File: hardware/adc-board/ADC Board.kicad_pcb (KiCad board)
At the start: 4 copper layers, 92.7 x 83.8 mm, 123 parts, among them J1 BHR-44-HUA, J10 BootJumper, J11 USB Header, J2 ST-LINK/V2, J3 USART3, J4 USART1, J5 UE27AC5410H, J6 54601-908WPLF, J7 AltPowerInput, J8 USBPowerJumper, J9 USART2, U0 STM32H743ZITx, U1 Opamp_Quad_Generic, U10 MCP1501T-20E/CHY, U13 3.3V Reg, U14 ISL83490, U2 Opamp_Quad_Generic, U29 AP2114HA-3.3TRG1, U3 Opamp_Quad_Generic, U4 Opamp_Quad_Generic, U5 Opamp_Quad_Generic, U6 Opamp_Quad_Generic, U7 MCP120-xxxxTT, U9 USBLC6-2SC6

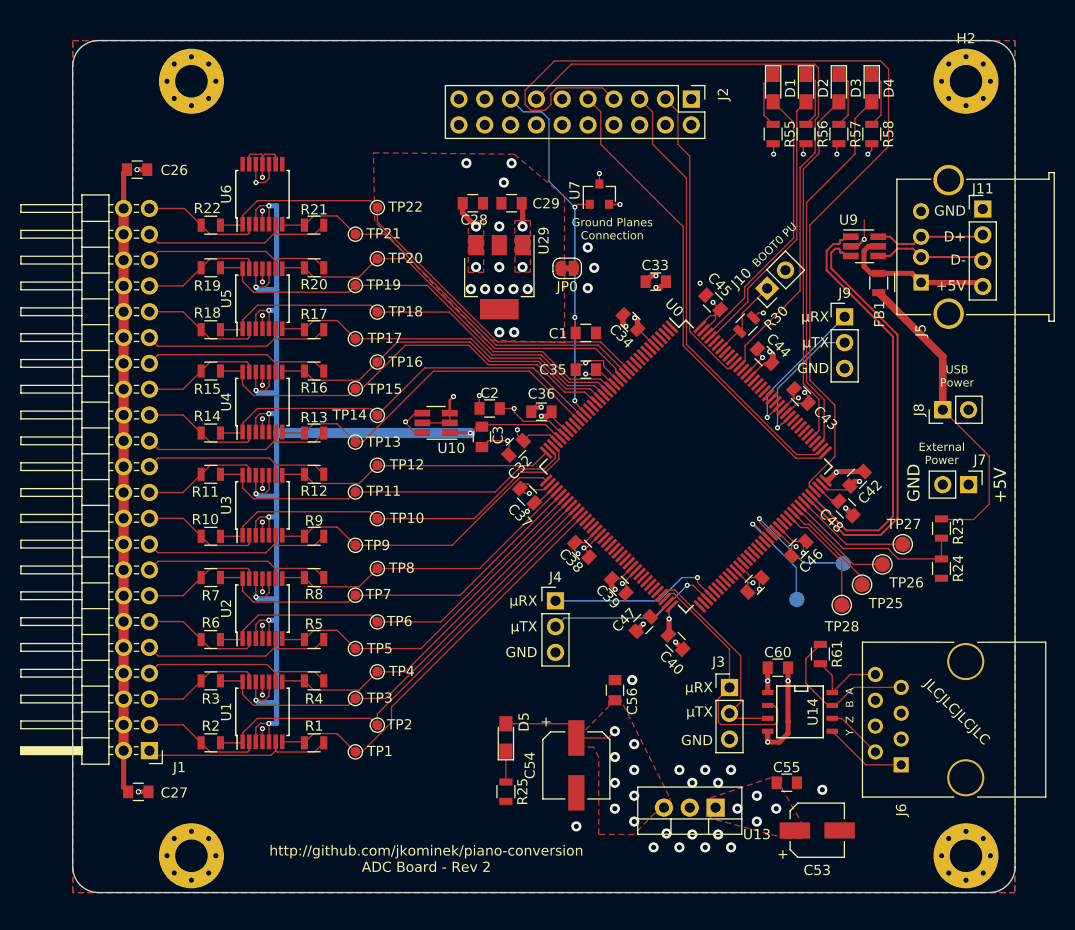
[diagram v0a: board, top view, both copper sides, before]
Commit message: Unified ground nets in schematic and layout.
* Rearranged the layers that pours are on.
* Added the keep-out zone separating analog and
  digital areas from each other.
* Tightened up placement of decoupling capacitors.
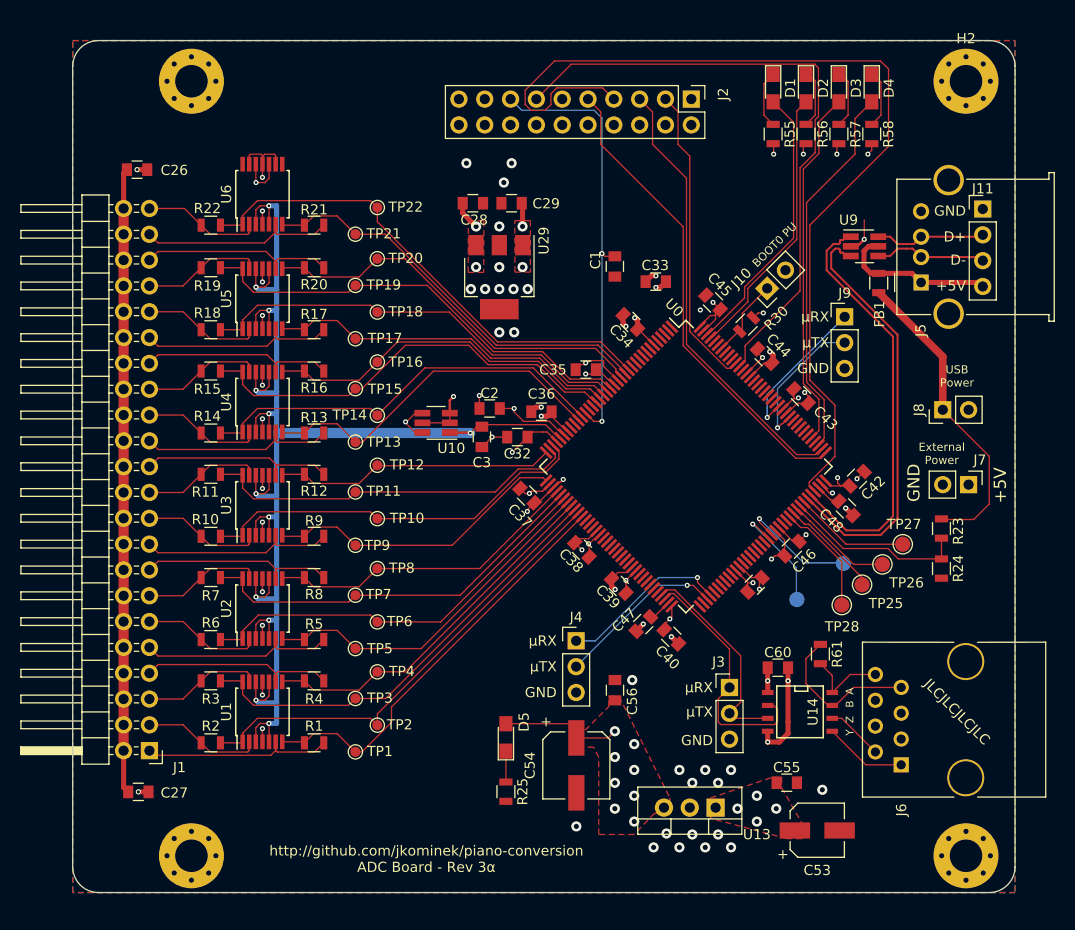
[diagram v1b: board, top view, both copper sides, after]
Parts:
- removed JP0: SolderJumper_2_Bridged, Jumper:SolderJumper-2_P1.3mm_Bridged_RoundedPad1.0x1.5mm
- removed U7: MCP120-xxxxTT, TO_SOT_Packages_SMD:SOT-23
- moved C1 7.14 mm to (85.1, 69.2), turned to -90 degrees
- moved J4 4.43 mm to (81.3, 106.0)
- moved C32 1.07 mm to (75.5, 86.0), turned to 180 degrees
- moved C46 0.68 mm to (102.5, 97.0)
- moved C40 0.67 mm to (90.6, 105.6)
- turned C42 to 45 degrees
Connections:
- C1 pad 2: GNDD -> GND
- C2 pad 2: GNDA -> GND
- C26 pad 1: GNDA -> GND
- C27 pad 1: GNDA -> GND
- C28 pad 2: GNDA -> GND
- C29 pad 2: GNDA -> GND
- C3 pad 2: GNDA -> GND
- C32 pad 2: GNDA -> GND
- C33 pad 2: GNDD -> GND
- C34 pad 2: GNDD -> GND
- C35 pad 2: GNDD -> GND
- C36 pad 2: GNDD -> GND
- C37 pad 2: GNDD -> GND
- C38 pad 2: GNDD -> GND
- C39 pad 2: GNDD -> GND
- C40 pad 2: GNDD -> GND
- C41 pad 2: GNDD -> GND
- C42 pad 2: GNDD -> GND
- C43 pad 2: GNDD -> GND
- C44 pad 2: GNDD -> GND
- C45 pad 2: GNDD -> GND
- C46 pad 2: GNDD -> GND
- C47 pad 2: GNDD -> GND
- C48 pad 2: GNDD -> GND
- C53 pad 2: GNDD -> GND
- C54 pad 2: GNDD -> GND
- C55 pad 2: GNDD -> GND
- C56 pad 2: GNDD -> GND
- C60 pad 2: GNDD -> GND
- H1 pad 1: GNDD -> GND
- H2 pad 1: GNDD -> GND
- H3 pad 1: GNDD -> GND
- H4 pad 1: GNDD -> GND
- J11 pad 1: GNDD -> GND
- J2 pad 10: GNDD -> GND
- J2 pad 12: GNDD -> GND
- J2 pad 14: GNDD -> GND
- J2 pad 16: GNDD -> GND
- J2 pad 18: GNDD -> GND
- J2 pad 20: GNDD -> GND
- J2 pad 4: GNDD -> GND
- J2 pad 6: GNDD -> GND
- J2 pad 8: GNDD -> GND
- J3 pad 3: GNDD -> GND
- J4 pad 3: GNDD -> GND
- J5 pad 4: GNDD -> GND
- J5 pad 5: GNDD -> GND
- J6 pad 4: GNDD -> GND
- J6 pad 6: GNDD -> GND
- J7 pad 2: GNDD -> GND
- J9 pad 3: GNDD -> GND
- R24 pad 2: GNDD -> GND
- R25 pad 2: GNDD -> GND
- R30 pad 2: GNDD -> GND
- R55 pad 2: GNDD -> GND
- R56 pad 2: GNDD -> GND
- R57 pad 2: GNDD -> GND
- R58 pad 2: GNDD -> GND
- U0 pad 107: GNDD -> GND
- U0 pad 120: GNDD -> GND
- U0 pad 130: GNDD -> GND
- U0 pad 16: GNDD -> GND
- U0 pad 31: GNDA -> GND
- U0 pad 38: GNDD -> GND
- U0 pad 51: GNDD -> GND
- U0 pad 61: GNDD -> GND
- U0 pad 83: GNDD -> GND
- U0 pad 94: GNDD -> GND
- U1 pad 11: GNDA -> GND
- U10 pad 2: GNDA -> GND
- U10 pad 3: GNDA -> GND
- U10 pad 5: GNDA -> GND
- U13 pad 2: GNDD -> GND
- U14 pad 4: GNDD -> GND
- U2 pad 11: GNDA -> GND
- U29 pad 2: GNDA -> GND
- U3 pad 11: GNDA -> GND
- U4 pad 11: GNDA -> GND
- U5 pad 11: GNDA -> GND
- U6 pad 11: GNDA -> GND
- U6 pad 13: GNDA -> GND
- U6 pad 9: GNDA -> GND
- U9 pad 2: GNDD -> GND
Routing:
- net GND: track 0.00 -> 92.8 mm, vias 0 -> 63
- net GNDD: track 64.5 -> 0.00 mm, vias 43 -> 0
- net GNDA: track 33.2 -> 0.00 mm, vias 23 -> 0
- net /NRST: track 38.1 -> 42.9 mm, vias 3 -> 2
- net +3V3: track 65.4 -> 62.1 mm
- added copper zone on In1.Cu, net +3.3VA
- added copper zone on In1.Cu, net +3V3
- added copper zone on In2.Cu, net +5V
- added copper zone on B.Cu, net GND
- added copper zone on F.Cu, net GND
- removed copper zone on In2.Cu, net +3.3VA
- removed copper zone on In2.Cu, net +3V3
- removed copper zone on B.Cu, net +5V
- removed copper zone on F.Cu, net GNDA
- removed copper zone on In1.Cu, net GNDA
- removed copper zone on F.Cu, net GNDD
- removed copper zone on In1.Cu, net GNDD
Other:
- board text added: "http://github.com/jkominek/piano-conversion ADC Board - Rev 3α"
- board text removed: "Ground Planes Connection"
- board text removed: "http://github.com/jkominek/piano-conversion ADC Board - Rev 2"

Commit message: More ADC board rev 3 changes, per issue #47
* 4.5V regulator for phototransistors
* new 3.3V regulator for analog section
* new 2.0V precision voltage reference
* Analog voltages and their distribution rearranged
* Tidied up traces on the left hand side, everything is nice and curvy now
* Adjusted USB ESD protection to be optional and/or support other parts
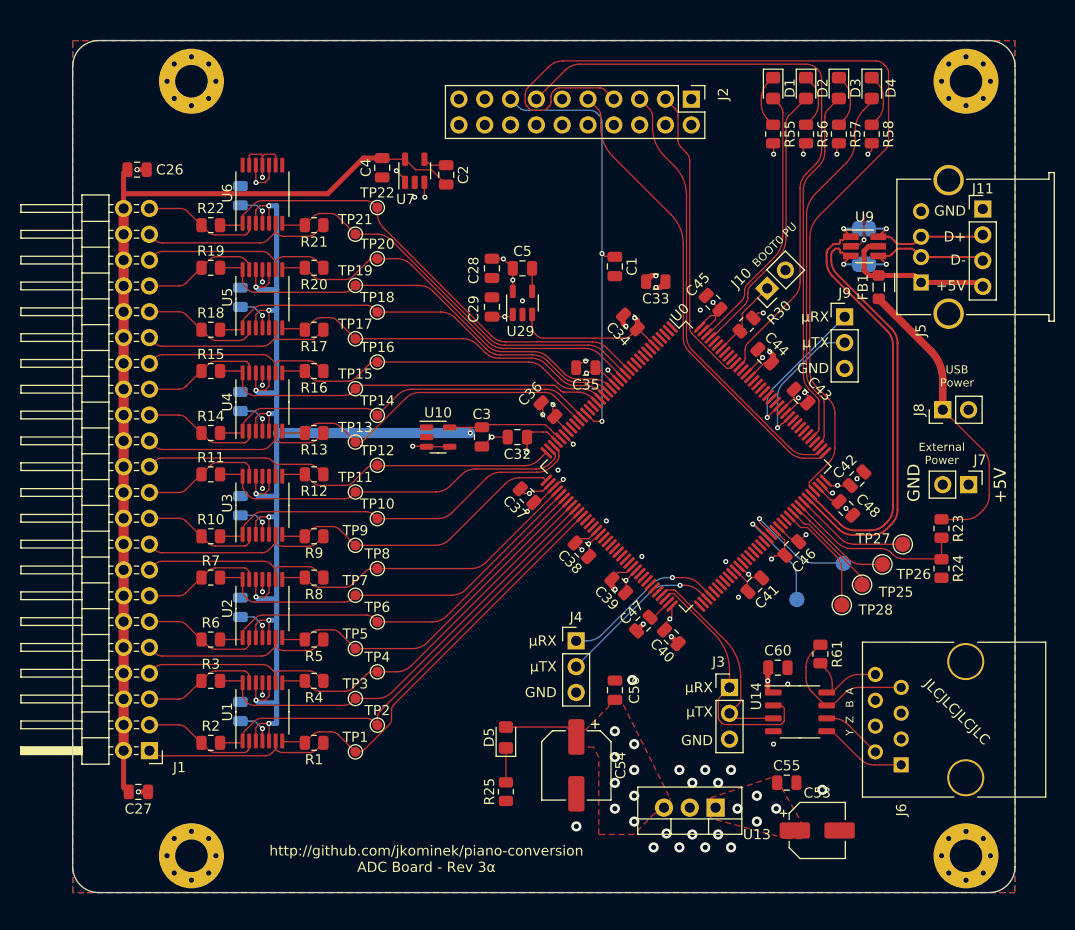
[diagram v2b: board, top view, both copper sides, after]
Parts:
- added C10: DC, Capacitor_SMD:C_0805_2012Metric, B.Cu at (48.2, 72.2)
- added C11: DC, Capacitor_SMD:C_0805_2012Metric, B.Cu at (48.2, 62.2)
- added C4: 1uF, Capacitor_SMD:C_0805_2012Metric, F.Cu at (62.2, 59.5)
- added C5: DNP, Capacitor_SMD:C_0805_2012Metric, F.Cu at (76.0, 69.4)
- added C6: DC, Capacitor_SMD:C_0805_2012Metric, B.Cu at (48.2, 113.0)
- added C7: DC, Capacitor_SMD:C_0805_2012Metric, B.Cu at (48.2, 102.8)
- added C8: DC, Capacitor_SMD:C_0805_2012Metric, B.Cu at (48.2, 92.8)
- added C9: DC, Capacitor_SMD:C_0805_2012Metric, B.Cu at (48.2, 82.5)
- added JP1: SolderJumper_2_Bridged, Jumper:SolderJumper-2_P1.3mm_Bridged_RoundedPad1.0x1.5mm, B.Cu at (109.6, 65.5)
- added JP2: SolderJumper_2_Bridged, Jumper:SolderJumper-2_P1.3mm_Bridged_RoundedPad1.0x1.5mm, B.Cu at (109.6, 69.0)
- added U7: LP2985AIM5-4.5/NOPB, Package_TO_SOT_SMD:SOT-23-5, F.Cu at (65.4, 59.8)
- C1, C26, C27, C32, C33, C34, C35, C36, C37, C38, C39, C40, C41, C42, C43, C44, C45, C46, C47, C48, C55, C56, C60: footprint Capacitors_SMD:C_0805 -> Capacitor_SMD:C_0805_2012Metric
- C2: value 2.2uF -> 1nF; footprint Capacitors_SMD:C_0805 -> Capacitor_SMD:C_0805_2012Metric
- C28, C29: value 4.7uF -> 1uF; footprint Capacitors_SMD:C_0805 -> Capacitor_SMD:C_0805_2012Metric
- C3: value 220pF -> 22nF; footprint Capacitors_SMD:C_0805 -> Capacitor_SMD:C_0805_2012Metric
- C53: footprint Capacitors_SMD:CP_Elec_5x5.3 -> Capacitor_SMD:CP_Elec_5x5.3
- C54: footprint Capacitors_SMD:CP_Elec_6.3x5.3 -> Capacitor_SMD:CP_Elec_6.3x5.3
- D1, D2, D3, D4, D5: footprint LEDs:LED_0805_HandSoldering -> LED_SMD:LED_0805_2012Metric_Pad1.15x1.40mm_HandSolder
- FB1: footprint Inductors_SMD:L_0805 -> Inductor_SMD:L_0805_2012Metric_Pad1.05x1.20mm_HandSolder
- H1, H2, H3, H4: footprint Mounting_Holes:MountingHole_3.2mm_M3_Pad_Via -> MountingHole:MountingHole_3.2mm_M3_Pad_Via
- R1, R10, R11, R12, R13, R14, R15, R16, R17, R18, R19, R2, R20, R21, R22, R23, R24, R25, R3, R30, R4, R5, R55, R56, R57, R58, R6, R61, R7, R8, R9: footprint Resistors_SMD:R_0805 -> Resistor_SMD:R_0805_2012Metric
- TP1, TP10, TP11, TP12, TP13, TP14, TP15, TP16, TP17, TP18, TP19, TP2, TP20, TP21, TP22, TP3, TP4, TP5, TP6, TP7, TP8, TP9: footprint Testpoint:TestPoint_Pad_D1.0mm -> TestPoint:TestPoint_Pad_D1.0mm
- TP23, TP24, TP25, TP26, TP27, TP28: footprint Testpoint:TestPoint_Pad_D1.5mm -> TestPoint:TestPoint_Pad_D1.5mm
- U0: footprint Housings_QFP:LQFP-144_20x20mm_Pitch0.5mm -> Package_QFP:TQFP-144_20x20mm_P0.5mm
- U1, U2, U3, U4, U5, U6: footprint Housings_SSOP:TSSOP-14_4.4x5mm_Pitch0.65mm -> Package_SO:TSSOP-14_4.4x5mm_P0.65mm
- U10: value MCP1501T-20E/CHY -> LM4120IM5-2.0/NOPB; footprint TO_SOT_Packages_SMD:SOT-23-6_Handsoldering -> Package_TO_SOT_SMD:SOT-23-5
- U14: footprint SMD_Packages:SOIC-8-N -> Package_SO:SOP-8_3.9x4.9mm_P1.27mm
- U29: value AP2114HA-3.3TRG1 -> NCP115ASN330T2G; footprint TO_SOT_Packages_SMD:SOT-223-3_TabPin2 -> Package_TO_SOT_SMD:SOT-23-5
- U9: footprint TO_SOT_Packages_SMD:SOT-23-6_Handsoldering -> Package_TO_SOT_SMD:SOT-23-6_Handsoldering
- moved C2 23.4 mm to (68.5, 60.2), turned to -90 degrees
- moved C29 10.4 mm to (73.0, 73.2), turned to 90 degrees
- moved C28 6.68 mm to (73.0, 69.4), turned to -90 degrees
- moved U29 3.40 mm to (76.0, 72.8), turned to 90 degrees
- moved U10 1.41 mm to (67.7, 86.0), turned to 0 degrees
- moved C36 0.66 mm to (78.5, 83.3), turned to 135 degrees
- moved FB1 0.41 mm to (111.0, 71.2)
- moved C35 0.19 mm to (82.2, 79.2)
- turned U14 to 0 degrees
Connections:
- C2 pad 1: +3.3VA -> Net-(C2-Pad1)
- C2 pad 2: GND -> +4V
- C26 pad 2: +3.3VA -> +4V
- C27 pad 2: +3.3VA -> +4V
- J1 pad 10: +3.3VA -> +4V
- J1 pad 12: +3.3VA -> +4V
- J1 pad 14: +3.3VA -> +4V
- J1 pad 16: +3.3VA -> +4V
- J1 pad 18: +3.3VA -> +4V
- J1 pad 2: +3.3VA -> +4V
- J1 pad 20: +3.3VA -> +4V
- J1 pad 22: +3.3VA -> +4V
- J1 pad 24: +3.3VA -> +4V
- J1 pad 26: +3.3VA -> +4V
- J1 pad 28: +3.3VA -> +4V
- J1 pad 30: +3.3VA -> +4V
- J1 pad 32: +3.3VA -> +4V
- J1 pad 34: +3.3VA -> +4V
- J1 pad 36: +3.3VA -> +4V
- J1 pad 38: +3.3VA -> +4V
- J1 pad 4: +3.3VA -> +4V
- J1 pad 40: +3.3VA -> +4V
- J1 pad 42: +3.3VA -> +4V
- J1 pad 44: +3.3VA -> +4V
- J1 pad 6: +3.3VA -> +4V
- J1 pad 8: +3.3VA -> +4V
- U10 pad 1: /VREF+ -> unconnected-(U10-Pad1)
- U10 pad 3: GND -> +3.3VA
- U10 pad 5: GND -> /VREF+
- U29 pad 3: +3.3VA -> +3V3
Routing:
- net +4V: track 0.00 -> 95.8 mm
- net +3.3VA: track 87.8 -> 42.1 mm
- net GND: track 92.8 -> 68.2 mm, vias 63 -> 57
- net +3V3: track 62.1 -> 67.2 mm
- net /Sen15: track 43.1 -> 39.7 mm
- net /USB_D-: track 11.1 -> 13.7 mm, vias 0 -> 1
- net /USB_D+: track 11.0 -> 13.6 mm, vias 0 -> 1
- net Net-(C2-Pad1): track 0.00 -> 2.39 mm
- net Net-(C5-Pad2): track 0.00 -> 2.26 mm
- net /Sen14: track 41.3 -> 39.2 mm
- net /Sen13: track 35.2 -> 33.2 mm
- net /Sen16: track 35.5 -> 33.6 mm
- net /USB_OTG_FS_D-: track 42.4 -> 44.3 mm, vias 0 -> 1
- net /USB_OTG_FS_D+: track 42.0 -> 43.9 mm, vias 0 -> 1
- net +5V: track 2.32 -> 3.63 mm
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- removed copper zone on F.Cu, net +3.3VA
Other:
- board text added: "Not power, just enable"

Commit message: ADC board layout tweaks; rearranged the various power planes
* Moved to standard plane layout of power, ground, ground, power,
  which I should've done from the start.
* Removed pads from the mounting holes, don't want to risk ground
  loops through the frame, there's no value.
* Adjusted the position of the 3.3VA regulator.
* Tweaked/tightened up a lot of traces, trying to keep them shorter.
* Bunch of extra vias stitching planes together.
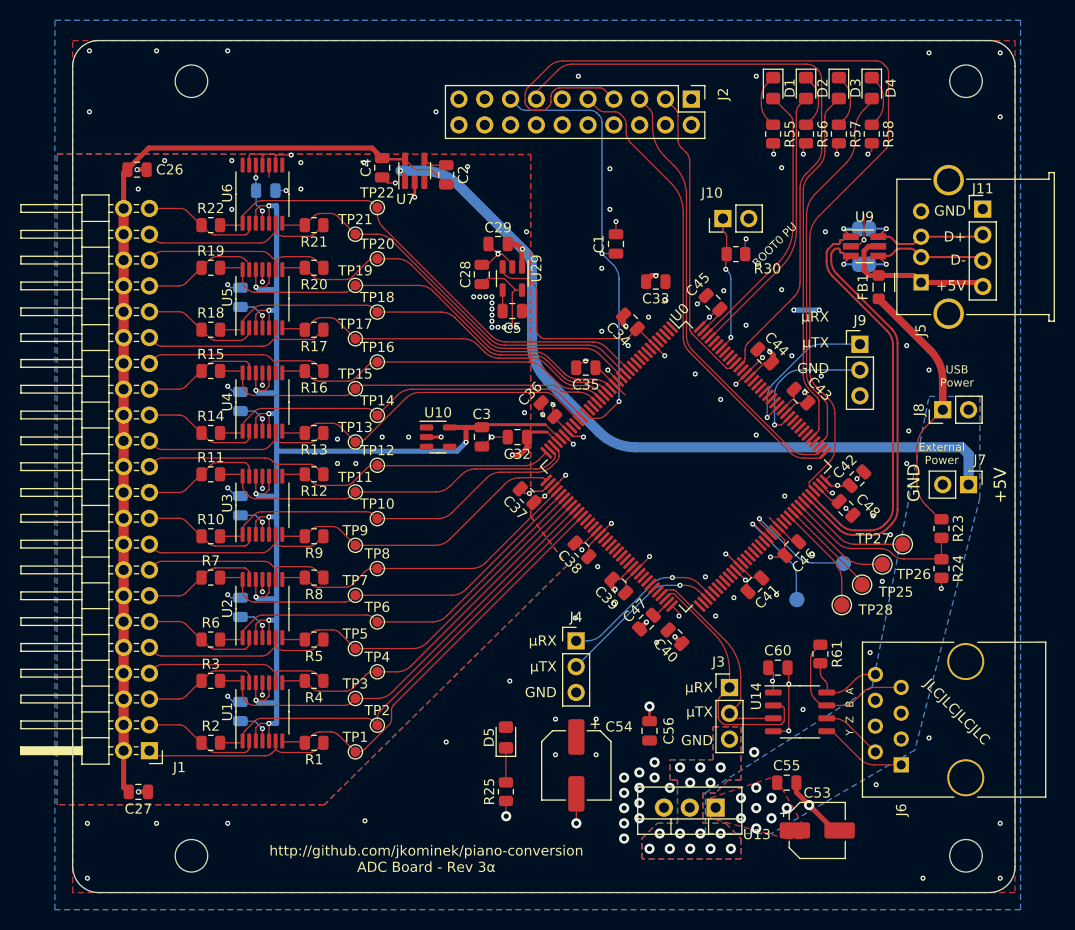
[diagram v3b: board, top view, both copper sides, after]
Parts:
- H1, H2, H3, H4: footprint MountingHole:MountingHole_3.2mm_M3_Pad_Via -> MountingHole:MountingHole_3.2mm_M3
- moved J10 8.14 mm to (95.7, 64.5), turned to 90 degrees
- moved R30 7.01 mm to (97.0, 68.0), turned to 0 degrees
- moved C29 6.23 mm to (73.6, 67.0), turned to 180 degrees
- moved C56 5.25 mm to (88.5, 114.9)
- moved C5 4.32 mm to (75.0, 73.6), turned to 180 degrees
- moved J9 3.08 mm to (109.2, 76.9)
- moved U29 2.60 mm to (75.0, 70.4), turned to -90 degrees
- moved C11 2.55 mm to (50.8, 61.8), turned to 0 degrees
- moved C1 2.22 mm to (85.2, 67.0), turned to 90 degrees
- moved C28 1.17 mm to (72.0, 70.0), turned to 90 degrees
- moved C47 0.37 mm to (88.2, 104.2)
- moved C40 0.35 mm to (91.0, 105.6)
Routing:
- net +5V: track 3.63 -> 80.5 mm, vias 6 -> 10
- net GND: track 68.2 -> 111.7 mm, vias 57 -> 66
- net +3V3: track 67.2 -> 75.7 mm, vias 24 -> 92
- net /BOOT0: track 7.83 -> 13.5 mm, vias 0 -> 2
- net /USB_VBUS: track 29.5 -> 26.0 mm
- net /JTCK: track 46.3 -> 47.4 mm
- net +3.3VA: track 42.1 -> 41.1 mm, vias 12 -> 36
- net /LED1: track 26.4 -> 27.2 mm
- net /NRST: track 42.8 -> 43.6 mm
- net /VREF+: track 148.9 -> 149.7 mm
- net /RS485/B: track 14.4 -> 15.1 mm
- net /USART2_TX: track 13.8 -> 14.4 mm
- net +4V: track 95.8 -> 95.2 mm
- net /USART2_RX: track 14.6 -> 15.2 mm
- added copper zone on B.Cu, net +3.3VA
- added copper zone on F.Cu, net +3.3VA
- added copper zone on B.Cu, net +3V3
- added copper zone on B.Cu, net +5V
- added copper zone on In1.Cu, net GND
- added copper zone on In2.Cu, net GND
- removed copper zone on In1.Cu, net +3.3VA
- removed copper zone on In1.Cu, net +3V3
- removed copper zone on In2.Cu, net +5V
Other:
- board text added: "We've got a bunch of copper and a pile of vias here, just in case somebody wants to run a linear regulator here instead of a switcher."

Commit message: Next revs of the important boards
Includes some tiny DRC tweaks for the LED power board.
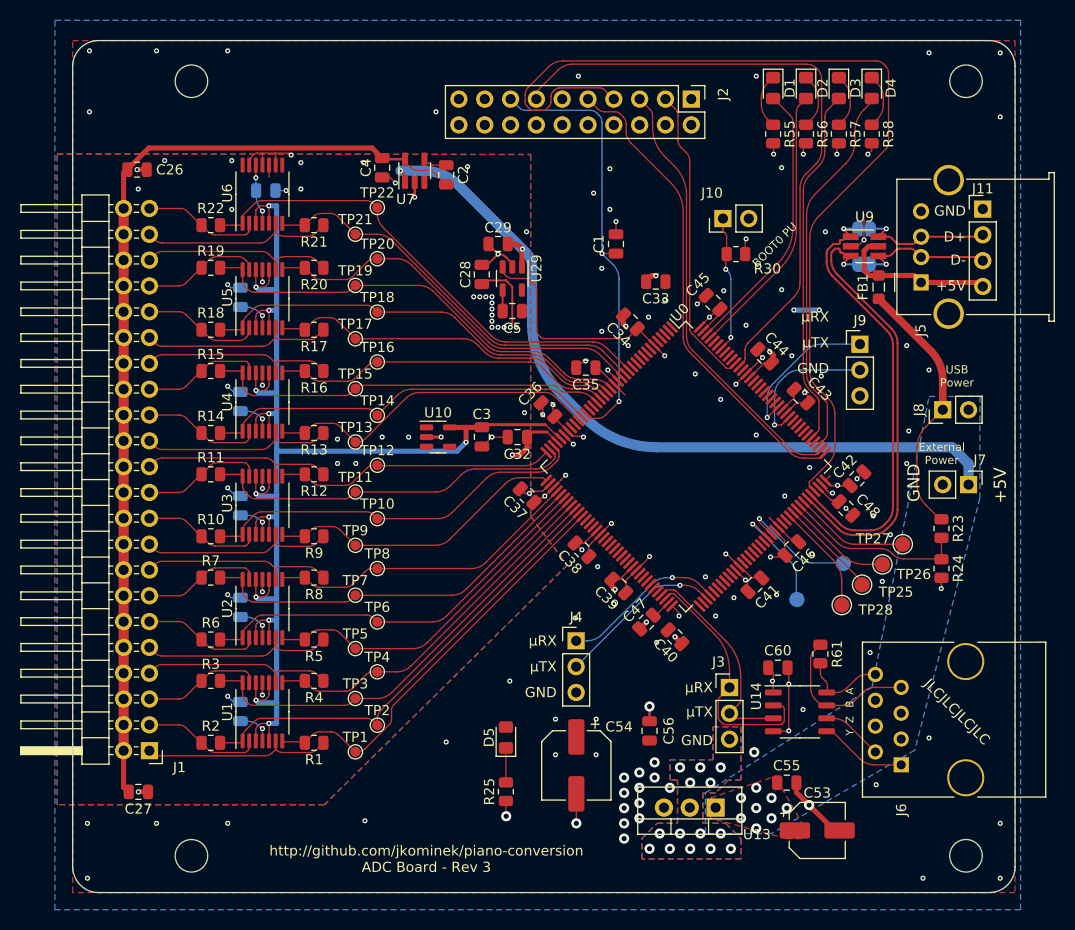
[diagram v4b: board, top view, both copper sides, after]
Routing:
- net +5V: track 80.5 -> 79.4 mm
- net +3.3VA: track 41.1 -> 40.4 mm
- net +3V3: vias 92 -> 93
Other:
- board text added: "http://github.com/jkominek/piano-conversion ADC Board - Rev 3"
- board text removed: "http://github.com/jkominek/piano-conversion ADC Board - Rev 3α"
